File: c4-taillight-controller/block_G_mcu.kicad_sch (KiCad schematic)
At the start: 1 part, among them U1 RP2040

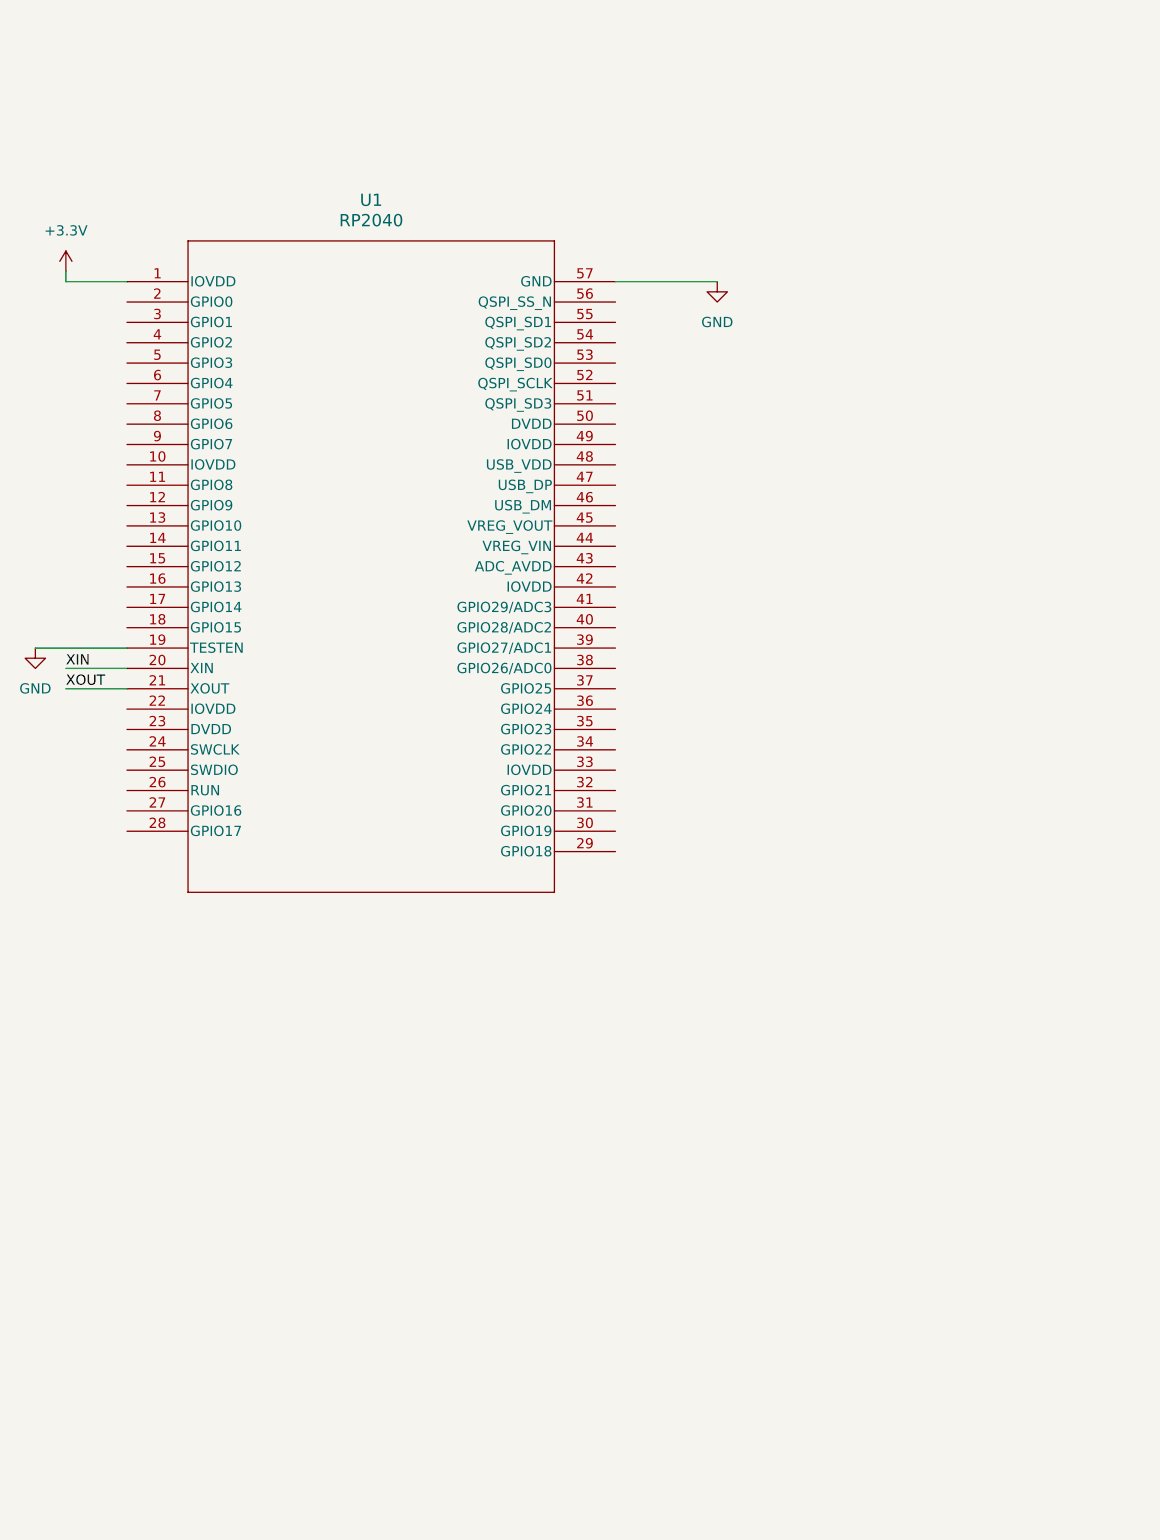
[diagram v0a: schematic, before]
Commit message: 8/13/2026 changes. using nRF52840 instead of RP2040
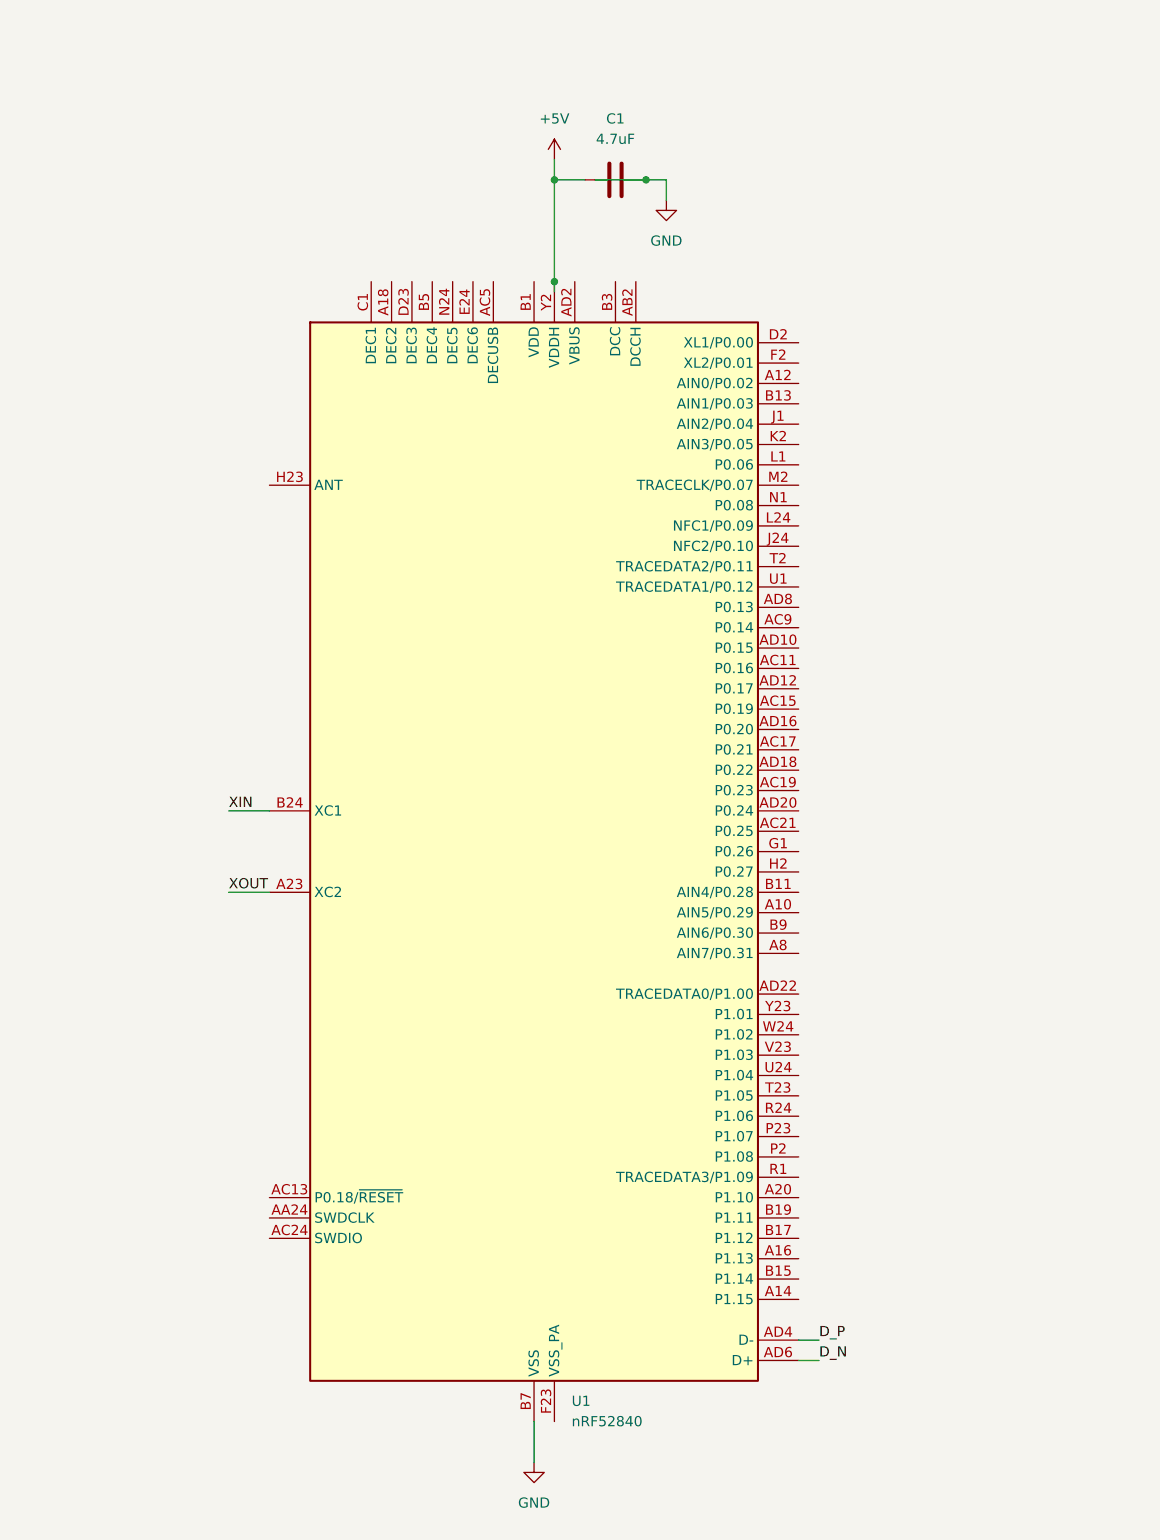
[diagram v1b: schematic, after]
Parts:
- removed U1: RP2040, IC57_RP2040, symbol RP2040:RP2040
- added C1: 4.7uF, symbol Device:C
- added U1: nRF52840, Package_DFN_QFN:Nordic_AQFN-73-1EP_7x7mm_P0.5mm, symbol MCU_Nordic:nRF52840
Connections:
- net GND: now also C1.2, U1.B7 (VSS), U1.EP (VSS)
- net XIN: now also U1.B24 (XC1)
- net XOUT: now also U1.A23 (XC2)
- new net: U1.A22 (VDD), U1.AD14 (VDD), U1.AD23 (VDD), U1.B1 (VDD), U1.W1 (VDD)
- new net +5V: C1.1, U1.Y2 (VDDH)
- new net D_N: U1.AD6 (D+)
- new net D_P: U1.AD4 (D-)

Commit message: 8/14/2026 began MCU layout schematic
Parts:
- added C2, C3: 12pF, symbol Device:C
- added C4, C5: 4.7uF, symbol Device:C
- added X1: 32MHz, symbol Device:Crystal
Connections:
- net +5V: now also C1.2; no longer C1.1
- net GND: now also C1.1, C2.1, C3.1, C4.2, C5.2; no longer C1.2
- net XIN: now also C2.2, X1.2
- net XOUT: now also C3.2, X1.1
- net VDD_nRF: now reaches U1.A22 (VDD), U1.AD14 (VDD), U1.AD23 (VDD), U1.B1 (VDD), U1.W1 (VDD)
- net VDD_nRF: now also C4.1
- net SWDCLK: now reaches U1.AA24 (SWDCLK)
- net RESET: now reaches U1.AC13 (P0.18/~{RESET})
- net SWDIO: now reaches U1.AC24 (SWDIO)
- net at U1.AC5 (DECUSB): now also C5.1
- net D_N renamed USB_P
- net D_P renamed USB_N
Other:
- moved on the sheet: C1, U1

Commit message: Added new nRF52840 module board. MDBT50Q - U1MV2
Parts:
- removed C1, C4, C5: 4.7uF, symbol Device:C
- removed C2, C3: 12pF, symbol Device:C
- removed U1: nRF52840, Package_DFN_QFN:Nordic_AQFN-73-1EP_7x7mm_P0.5mm, symbol MCU_Nordic:nRF52840
- removed X1: 32MHz, symbol Device:Crystal
